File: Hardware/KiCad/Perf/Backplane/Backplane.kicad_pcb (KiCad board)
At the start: 2 copper layers, 99.1 x 73.7 mm, 10 parts, among them P1 CONN_02X20, P10 POWER, P2 CONN_02X20, P3 CONN_02X03, P4 AUX 3, P5 AUX 2, P6 AUX 1, P7 COMMUNICATION, P8 LIGHT, P9 MANIPULTOR

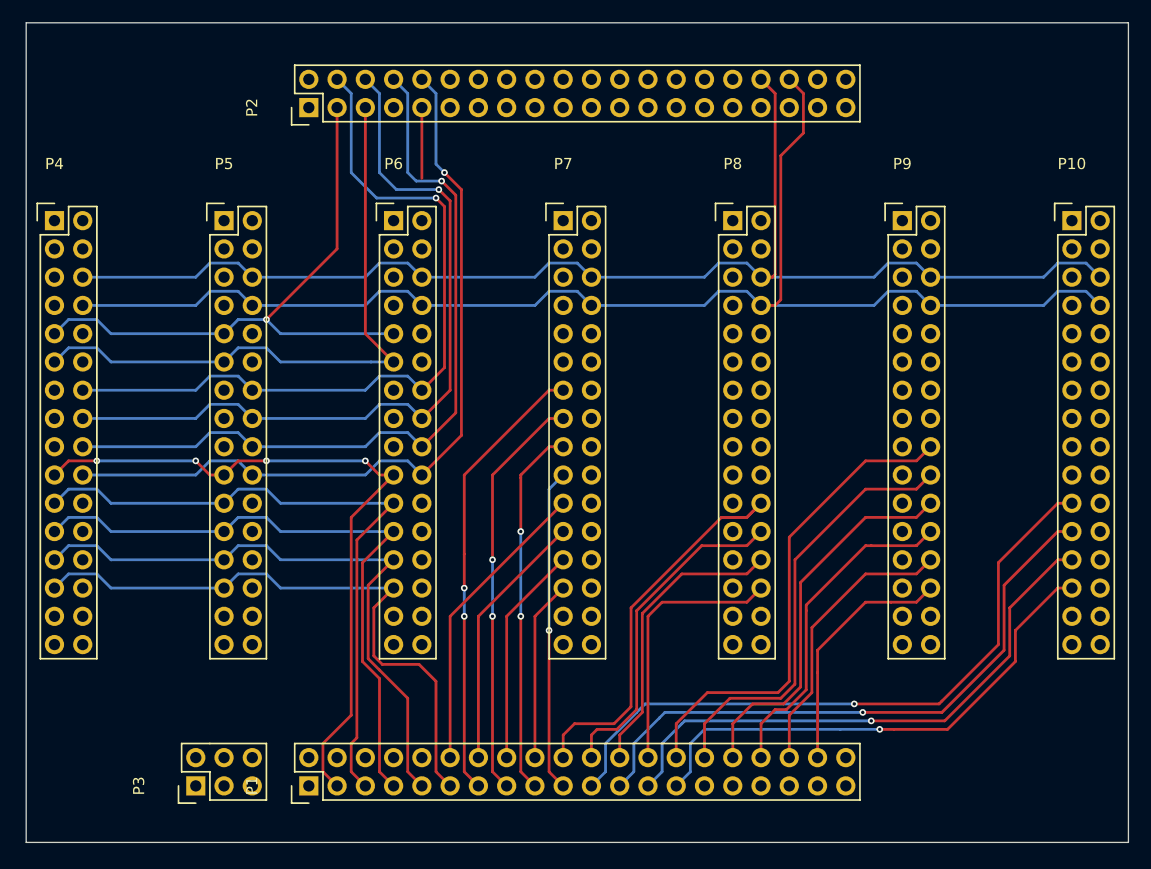
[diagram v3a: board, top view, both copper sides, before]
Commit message: completed backplane pcb
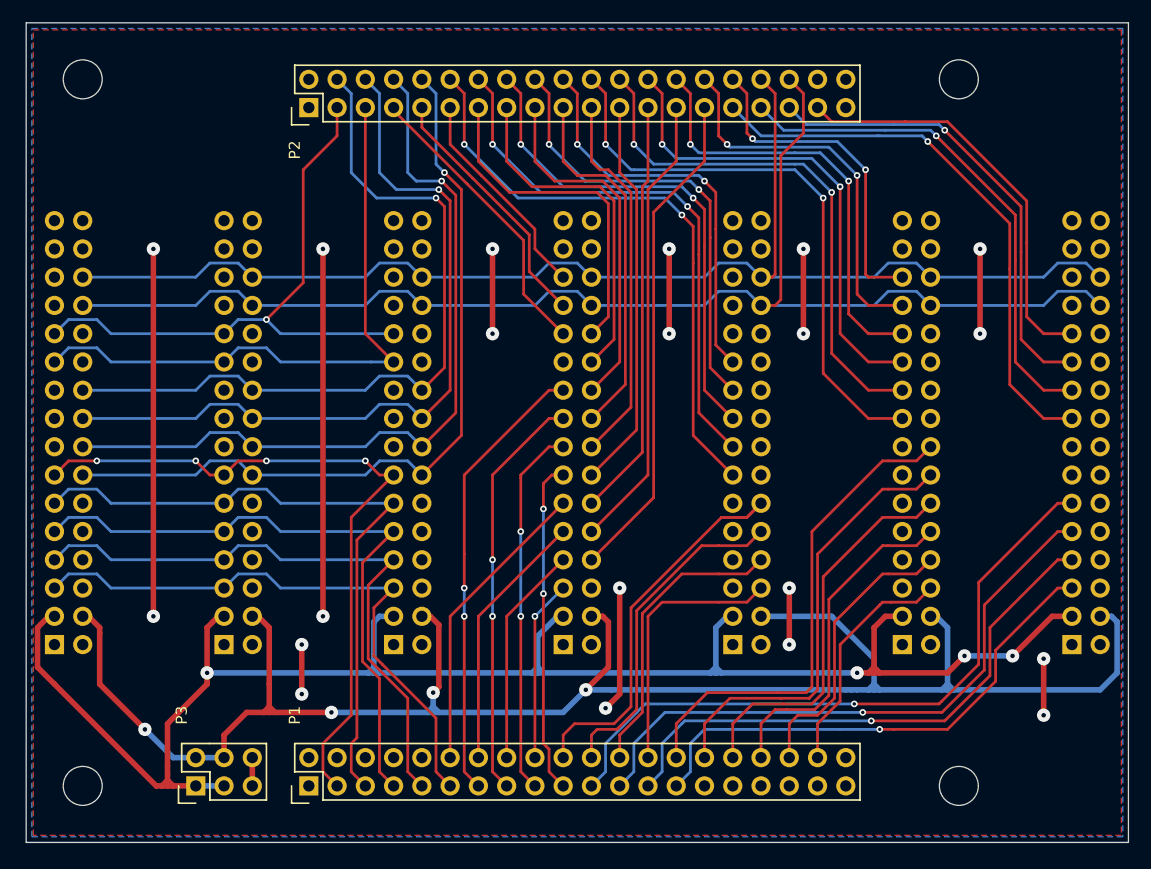
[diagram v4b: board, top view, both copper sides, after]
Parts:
- added ?: , Mounting_Holes:MountingHole_3-5mm, F.Cu at (124.5, 58.4)
- added ?: , Mounting_Holes:MountingHole_3-5mm, F.Cu at (124.5, 121.9)
- added ?: , Mounting_Holes:MountingHole_3-5mm, F.Cu at (45.7, 121.9)
- added ?: , Mounting_Holes:MountingHole_3-5mm, F.Cu at (45.7, 58.4)
- P10, P4, P5, P6, P7, P8, P9: moved to B.Cu
- moved P10 38.1 mm to (134.6, 109.2)
- moved P4 38.1 mm to (43.2, 109.2)
- moved P5 38.1 mm to (58.4, 109.2)
- moved P6 38.1 mm to (73.7, 109.2)
- moved P7 38.1 mm to (88.9, 109.2)
- moved P8 38.1 mm to (104.1, 109.2)
- moved P9 38.1 mm to (119.4, 109.2)
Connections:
- P1 pad 10: I2C_2_SDA -> Net-(P1-Pad10)
- P1 pad 8: I2C_2_SCL -> Net-(P1-Pad8)
- P10 pad 11: GPIO_8 -> ADC_10
- P10 pad 13: GPIO_9 -> Net-(P10-Pad13)
- P10 pad 15: GPIO_10 -> Net-(P10-Pad15)
- P10 pad 17: Net-(P10-Pad17) -> GPIO_7
- P10 pad 19: Net-(P10-Pad19) -> GPIO_8
- P10 pad 21: ADC_10 -> GPIO_9
- P10 pad 23: ADC_11 -> GPIO_10
- P10 pad 25: ADC_12 -> Net-(P10-Pad25)
- P10 pad 26: Net-(P10-Pad26) -> I2C_2_SDA
- P10 pad 27: ADC_13 -> Net-(P10-Pad27)
- P10 pad 28: Net-(P10-Pad28) -> I2C_2_SCL
- P10 pad 5: Net-(P10-Pad5) -> ADC_13
- P10 pad 6: I2C_2_SCL -> Net-(P10-Pad6)
- P10 pad 7: Net-(P10-Pad7) -> ADC_12
- P10 pad 8: I2C_2_SDA -> Net-(P10-Pad8)
- P10 pad 9: GPIO_7 -> ADC_11
- P4 pad 11: GPIO_28 -> GPIO_12
- P4 pad 13: Net-(P4-Pad13) -> GPIO_11
- P4 pad 14: GPIO_21 -> GPIO_24
- P4 pad 16: GPIO_22 -> GPIO_23
- P4 pad 18: GPIO_23 -> GPIO_22
- P4 pad 19: GPIO_11 -> Net-(P4-Pad19)
- P4 pad 20: GPIO_24 -> GPIO_21
- P4 pad 21: GPIO_12 -> GPIO_28
- P4 pad 23: GPIO_13 -> GPIO_29
- P4 pad 25: GPIO_14 -> Net-(P4-Pad25)
- P4 pad 26: Net-(P4-Pad26) -> I2C_2_SDA
- P4 pad 27: GPIO_15 -> Net-(P4-Pad27)
- P4 pad 28: Net-(P4-Pad28) -> I2C_2_SCL
- P4 pad 5: Net-(P4-Pad5) -> GPIO_15
- P4 pad 6: I2C_2_SCL -> Net-(P4-Pad6)
- P4 pad 7: Net-(P4-Pad7) -> GPIO_14
- P4 pad 8: I2C_2_SDA -> Net-(P4-Pad8)
- P4 pad 9: GPIO_29 -> GPIO_13
- P5 pad 11: GPIO_28 -> GPIO_12
- P5 pad 13: Net-(P5-Pad13) -> GPIO_11
- P5 pad 14: GPIO_21 -> GPIO_24
- P5 pad 16: GPIO_22 -> GPIO_23
- P5 pad 18: GPIO_23 -> GPIO_22
- P5 pad 19: GPIO_11 -> Net-(P5-Pad19)
- P5 pad 20: GPIO_24 -> GPIO_21
- P5 pad 21: GPIO_12 -> GPIO_28
- P5 pad 23: GPIO_13 -> GPIO_29
- P5 pad 25: GPIO_14 -> Net-(P5-Pad25)
- P5 pad 26: Net-(P5-Pad26) -> I2C_2_SDA
- P5 pad 27: GPIO_15 -> Net-(P5-Pad27)
- P5 pad 28: Net-(P5-Pad28) -> I2C_2_SCL
- P5 pad 5: Net-(P5-Pad5) -> GPIO_15
- P5 pad 6: I2C_2_SCL -> Net-(P5-Pad6)
- P5 pad 7: Net-(P5-Pad7) -> GPIO_14
- P5 pad 8: I2C_2_SDA -> Net-(P5-Pad8)
- P5 pad 9: GPIO_29 -> GPIO_13
- P6 pad 11: GPIO_28 -> GPIO_12
- P6 pad 13: Net-(P6-Pad13) -> GPIO_11
- P6 pad 14: GPIO_21 -> GPIO_24
- P6 pad 16: GPIO_22 -> GPIO_23
- P6 pad 18: GPIO_23 -> GPIO_22
- P6 pad 19: GPIO_11 -> Net-(P6-Pad19)
- P6 pad 20: GPIO_24 -> GPIO_21
- P6 pad 21: GPIO_12 -> GPIO_28
- P6 pad 23: GPIO_13 -> GPIO_29
- P6 pad 25: GPIO_14 -> Net-(P6-Pad25)
- P6 pad 26: Net-(P6-Pad26) -> I2C_2_SDA
- P6 pad 27: GPIO_15 -> Net-(P6-Pad27)
- P6 pad 28: Net-(P6-Pad28) -> I2C_2_SCL
- P6 pad 5: Net-(P6-Pad5) -> GPIO_15
- P6 pad 6: I2C_2_SCL -> Net-(P6-Pad6)
- P6 pad 7: Net-(P6-Pad7) -> GPIO_14
- P6 pad 8: I2C_2_SDA -> Net-(P6-Pad8)
- P6 pad 9: GPIO_29 -> GPIO_13
- P7 pad 10: USART_2_CK -> UART_4_RX
- P7 pad 11: Net-(P7-Pad11) -> SPI_1_NSS
- P7 pad 12: USART_2_RX -> UART_5_TX
- P7 pad 13: USART_3_TX -> USART_3_CTS
- P7 pad 14: USART_2_TX -> UART_5_RX
- P7 pad 15: USART_3_RX -> USART_3_CK
- P7 pad 16: USART_2_RTS -> USART_2_CTS
- P7 pad 17: USART_3_CK -> USART_3_RX
- P7 pad 18: USART_2_CTS -> USART_2_RTS
- P7 pad 19: USART_3_CTS -> USART_3_TX
- P7 pad 20: UART_5_RX -> USART_2_TX
- P7 pad 21: SPI_1_NSS -> Net-(P7-Pad21)
- P7 pad 22: UART_5_TX -> USART_2_RX
- P7 pad 23: SPI_1_SCK -> GPIO_27
- P7 pad 24: UART_4_RX -> USART_2_CK
- P7 pad 25: SPI_1_MSIO -> GPIO_26
- P7 pad 26: UART_4_TX -> I2C_2_SDA
- P7 pad 27: SPI_1_MOSI -> GPIO_25
- P7 pad 28: Net-(P7-Pad28) -> I2C_2_SCL
- P7 pad 5: GPIO_27 -> SPI_1_MOSI
- P7 pad 6: I2C_2_SCL -> Net-(P7-Pad6)
- P7 pad 7: GPIO_26 -> SPI_1_MSIO
- P7 pad 8: I2C_2_SDA -> UART_4_TX
- P7 pad 9: GPIO_25 -> SPI_1_SCK
- P8 pad 10: Net-(P8-Pad10) -> TIM_2_CH_2
- P8 pad 12: GPIO_20 -> TIM_2_CH_1
- P8 pad 13: Net-(P8-Pad13) -> GPIO_20
- P8 pad 14: GPIO_19 -> Net-(P8-Pad14)
- P8 pad 15: Net-(P8-Pad15) -> GPIO_19
- P8 pad 16: GPIO_18 -> Net-(P8-Pad16)
- P8 pad 17: Net-(P8-Pad17) -> GPIO_18
- P8 pad 18: GPIO_17 -> Net-(P8-Pad18)
- P8 pad 19: Net-(P8-Pad19) -> GPIO_17
- P8 pad 20: GPIO_16 -> Net-(P8-Pad20)
- P8 pad 21: Net-(P8-Pad21) -> GPIO_16
- P8 pad 22: TIM_2_CH_1 -> Net-(P8-Pad22)
- P8 pad 24: TIM_2_CH_2 -> Net-(P8-Pad24)
- P8 pad 26: TIM_2_CH_3 -> I2C_2_SDA
- P8 pad 28: TIM_2_CH_4 -> I2C_2_SCL
- P8 pad 6: I2C_2_SCL -> TIM_2_CH_4
- P8 pad 8: I2C_2_SDA -> TIM_2_CH_3
- P9 pad 10: Net-(P9-Pad10) -> TIM_12_CH_2
- P9 pad 11: GPIO_3 -> Net-(P9-Pad11)
- P9 pad 12: Net-(P9-Pad12) -> TIM_12_CH_1
- P9 pad 13: GPIO_4 -> Net-(P9-Pad13)
- P9 pad 14: Net-(P9-Pad14) -> TIM_14
- P9 pad 15: GPIO_5 -> Net-(P9-Pad15)
- P9 pad 16: Net-(P9-Pad16) -> TIM_13
- P9 pad 17: Net-(P9-Pad17) -> GPIO_0
- P9 pad 18: TIM_13 -> Net-(P9-Pad18)
- P9 pad 19: Net-(P9-Pad19) -> GPIO_1
- P9 pad 20: TIM_14 -> Net-(P9-Pad20)
- P9 pad 21: Net-(P9-Pad21) -> GPIO_2
- P9 pad 22: TIM_12_CH_1 -> Net-(P9-Pad22)
- P9 pad 23: Net-(P9-Pad23) -> GPIO_3
- P9 pad 24: TIM_12_CH_2 -> Net-(P9-Pad24)
- P9 pad 25: Net-(P9-Pad25) -> GPIO_4
- P9 pad 26: TIM_15_CH_1 -> I2C_2_SDA
- P9 pad 27: Net-(P9-Pad27) -> GPIO_5
- P9 pad 28: TIM_15_CH_2 -> I2C_2_SCL
- P9 pad 5: GPIO_0 -> Net-(P9-Pad5)
- P9 pad 6: I2C_2_SCL -> TIM_15_CH_2
- P9 pad 7: GPIO_1 -> Net-(P9-Pad7)
- P9 pad 8: I2C_2_SDA -> TIM_15_CH_1
- P9 pad 9: GPIO_2 -> Net-(P9-Pad9)
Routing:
- net +5V: track 0.00 -> 168.3 mm, vias 0 -> 4
- net +3V3: track 0.00 -> 157.5 mm, vias 0 -> 4
- net (no net): track 0.00 -> 122.4 mm, vias 0 -> 20
- net GPIO_20: track 0.00 -> 53.8 mm, vias 0 -> 2
- net GPIO_0: track 0.00 -> 52.5 mm, vias 0 -> 2
- net GPIO_7: track 0.00 -> 50.5 mm, vias 0 -> 1
- net GPIO_19: track 0.00 -> 49.5 mm, vias 0 -> 2
- net GPIO_1: track 0.00 -> 48.1 mm, vias 0 -> 2
- net GPIO_8: track 0.00 -> 46.2 mm, vias 0 -> 1
- net GPIO_18: track 0.00 -> 45.1 mm, vias 0 -> 2
- net UART_4_TX: track 0.00 -> 44.8 mm
- net GPIO_2: track 0.00 -> 44.0 mm, vias 0 -> 2
- net GPIO_9: track 0.00 -> 41.9 mm, vias 0 -> 1
- net UART_4_RX: track 0.00 -> 41.3 mm
- net GPIO_17: track 0.00 -> 41.0 mm, vias 0 -> 2
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- added copper zone on F.Cu, net (none)
- added copper zone on B.Cu, net GND
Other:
- net class Power added: clearance 0.4, trace_width 0.5, via_dia 1.2, via_drill 0.4
- board text added: "AUX 1"
- board text added: "AUX 2"
- board text added: "AUX 3"
- board text added: "COMMUNICATION"
- board text added: "LIGHT"
- board text added: "MANIPULATOR"
- board text added: "POWER"

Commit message: Created gerber files for ordering
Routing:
- net GND: track 2.54 -> 588.0 mm, vias 0 -> 16
- net (no net): track 122.4 -> 0.00 mm, vias 20 -> 0
